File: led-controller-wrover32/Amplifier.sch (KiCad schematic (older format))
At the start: 5 parts, among them J11 Conn_01x02, U5 MAX98357A

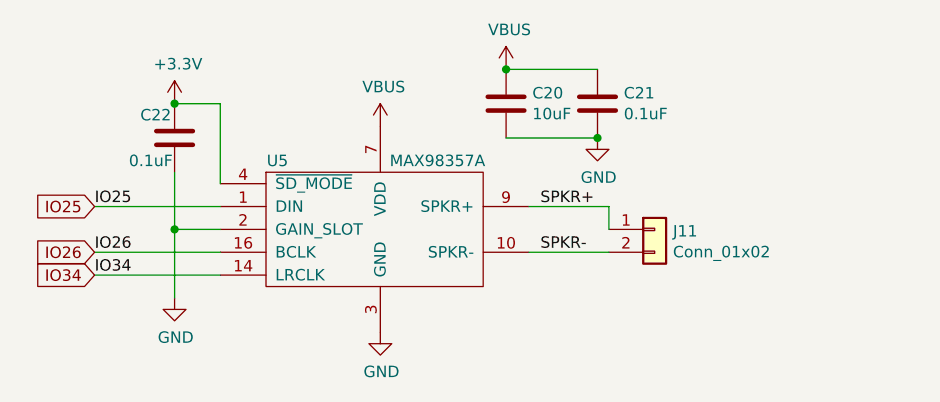
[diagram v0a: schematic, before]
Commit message: Fixed microphone, fan PWM and speaker
The ground was not hooked up to the microphone due to an issue with the
footprint.

The PWM pin was also used by the microphone.  Moved PWM pin to IO 5 which is
also shared with 5V output.

The speaker LR clock was using IO34 which is input only.  Moved to IO33 which
is also shared with a 5V output.

Updated revision to 3.0.1.
Fixed page settings, updated dates and revisions.

Signed-off-by: Aaron Williams <aaron.w2@gmail.com>
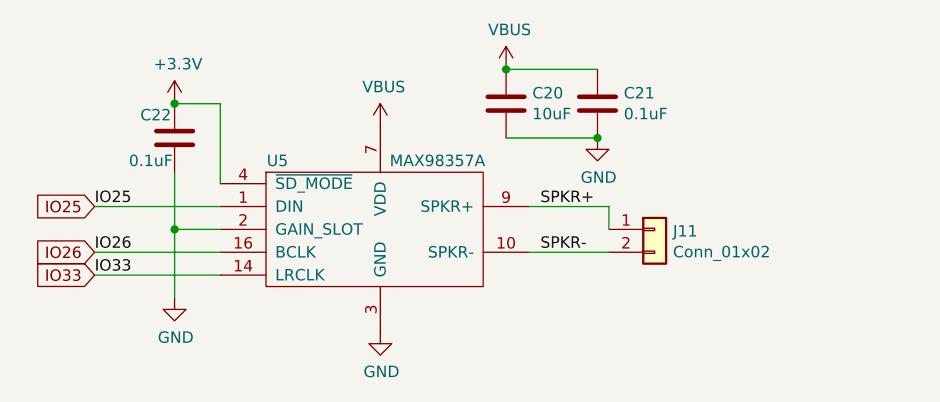
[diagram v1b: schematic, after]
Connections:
- net IO34 renamed IO33
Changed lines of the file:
@@
 	3200 3400 2650 3400
 Text Label 2650 3400 0    50   ~ 0
-IO34
+IO33
 Text GLabel 2650 3100 0    50   Input ~ 0
 IO25
@@
 IO26
 Text GLabel 2650 3400 0    50   Input ~ 0
-IO34
+IO33
 $Comp
 L Device:C C22

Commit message: Minor changes.
Signed-off-by: Aaron Williams <aaron.w2@gmail.com>
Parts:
- C20: MFR (none) -> Samsung; MPN (none) -> CL21B106KOQNNNE; SPN (none) -> 1276-2872-1-ND; SPR (none) -> Digikey; SPURL (none) -> -
- C21, C22: MFR (none) -> AVX; MPN (none) -> 06035C104K4Z4A; SPN (none) -> 478-10679-1-ND; SPR (none) -> Digikey; SPURL (none) -> -
- J11: value Conn_01x02 -> BM02B-SRSS-TB(LF)(SN)
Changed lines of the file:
@@
 U 1 1 5DB543D3
 P 3900 3200
-F 0 "U5" H 3450 3500 50  0000 C CNN
-F 1 "MAX98357A" H 4150 3500 50  0000 C CNN
-F 2 "Aaron:VQFN-16-1EP_3x3mm_P0.5mm_EP1.68x1.68mm" H 3900 3200 50  0001 C CNN
-F 3 "https://datasheets.maximintegrated.com/en/ds/MAX98357A-MAX98357B.pdf" H 3900 3200 50  0001 C CNN
-F 4 "Maxim Integrated" H 3900 3200 50  0001 C CNN "MFR"
-F 5 "MAX98357AETE+T" H 3900 3200 50  0001 C CNN "MPN"
-F 6 "Digikey" H 3900 3200 50  0001 C CNN "SPR"
-F 7 "MAX98357AETE+TCT-ND" H 3900 3200 50  0001 C CNN "SPN"
-F 8 "https://www.digikey.com/products/en/integrated-circuits-ics/linear-amplifiers-audio/742?k=MAX98357A&k=&pkeyword=MAX98357A&sv=0&pv7=2&pv1291=108687&pv16=108891&sf=0&FV=-8%7C742&quantity=&ColumnSort=0&page=1&pageSize=500" H 3900 3200 50  0001 C CNN "SPURL"
+F 0 "U5" H 3450 3500 50 0000 C CNN
+F 1 "MAX98357A" H 4150 3500 50 0000 C CNN
+F 2 "Aaron:VQFN-16-1EP_3x3mm_P0.5mm_EP1.68x1.68mm" H 3900 3200 50 0001 C CNN
+F 3 "https://datasheets.maximintegrated.com/en/ds/MAX98357A-MAX98357B.pdf" H 3900 3200 50 0001 C CNN
+F 4 "Maxim Integrated" H 3900 3200 50 0001 C CNN "MFR"
+F 5 "MAX98357AETE+T" H 3900 3200 50 0001 C CNN "MPN"
+F 6 "Digikey" H 3900 3200 50 0001 C CNN "SPR"
+F 7 "MAX98357AETE+TCT-ND" H 3900 3200 50 0001 C CNN "SPN"
+F 8 "https://www.digikey.com/products/en/integrated-circuits-ics/linear-amplifiers-audio/742?k=MAX98357A&k=&pkeyword=MAX98357A&sv=0&pv7=2&pv1291=108687&pv16=108891&sf=0&FV=-8%7C742&quantity=&ColumnSort=0&page=1&pageSize=500" H 3900 3200 50 0001 C CNN "SPURL"
 	1    3900 3200
 	1    0    0    -1
@@
 U 1 1 5DB55B9D
 P 4450 2650
-F 0 "C20" H 4565 2696 50  0000 L CNN
-F 1 "10uF" H 4565 2605 50  0000 L CNN
-F 2 "Capacitor_SMD:C_0805_2012Metric" H 4488 2500 50  0001 C CNN
-F 3 "~" H 4450 2650 50  0001 C CNN
+F 0 "C20" H 4565 2696 50 0000 L CNN
+F 1 "10uF" H 4565 2605 50 0000 L CNN
+F 2 "Capacitor_SMD:C_0805_2012Metric" H 4488 2500 50 0001 C CNN
+F 3 "http://www.samsungsem.com/kr/support/product-search/mlcc/CL21B106KOQNNNE.jsp" H 4450 2650 50 0001 C CNN
+F 4 "Samsung" H 0 0 50 0001 C CNN "MFR"
+F 5 "CL21B106KOQNNNE" H 0 0 50 0001 C CNN "MPN"
+F 6 "Digikey" H 0 0 50 0001 C CNN "SPR"
+F 7 "1276-2872-1-ND" H 0 0 50 0001 C CNN "SPN"
+F 8 "-" H 0 0 50 0001 C CNN "SPURL"
 	1    4450 2650
 	1    0    0    -1
@@
 U 1 1 5DB56E4D
 P 4850 2650
-F 0 "C21" H 4965 2696 50  0000 L CNN
-F 1 "0.1uF" H 4965 2605 50  0000 L CNN
-F 2 "Capacitor_SMD:C_0603_1608Metric" H 4888 2500 50  0001 C CNN
-F 3 "~" H 4850 2650 50  0001 C CNN
+F 0 "C21" H 4965 2696 50 0000 L CNN
+F 1 "0.1uF" H 4965 2605 50 0000 L CNN
+F 2 "Capacitor_SMD:C_0603_1608Metric" H 4888 2500 50 0001 C CNN
+F 3 "http://datasheets.avx.com/FlexitermMLCC.pdf" H 4850 2650 50 0001 C CNN
+F 4 "AVX" H 0 0 50 0001 C CNN "MFR"
+F 5 "06035C104K4Z4A" H 0 0 50 0001 C CNN "MPN"
+F 6 "Digikey" H 0 0 50 0001 C CNN "SPR"
+F 7 "478-10679-1-ND" H 0 0 50 0001 C CNN "SPN"
+F 8 "-" H 0 0 50 0001 C CNN "SPURL"
 	1    4850 2650
 	1    0    0    -1
@@
 U 1 1 5DB5770E
 P 3900 3650
-F 0 "#PWR0116" H 3900 3400 50  0001 C CNN
-F 1 "GND" H 3905 3477 50  0000 C CNN
-F 2 "" H 3900 3650 50  0001 C CNN
-F 3 "" H 3900 3650 50  0001 C CNN
+F 0 "#PWR0116" H 3900 3400 50 0001 C CNN
+F 1 "GND" H 3905 3477 50 0000 C CNN
+F 2 "" H 3900 3650 50 0001 C CNN
+F 3 "" H 3900 3650 50 0001 C CNN
 	1    3900 3650
 	1    0    0    -1
@@
 U 1 1 5DB58235
 P 3000 3500
-F 0 "#PWR0117" H 3000 3250 50  0001 C CNN
-F 1 "GND" H 3005 3327 50  0000 C CNN
-F 2 "" H 3000 3500 50  0001 C CNN
-F 3 "" H 3000 3500 50  0001 C CNN
+F 0 "#PWR0117" H 3000 3250 50 0001 C CNN
+F 1 "GND" H 3005 3327 50 0000 C CNN
+F 2 "" H 3000 3500 50 0001 C CNN
+F 3 "" H 3000 3500 50 0001 C CNN
 	1    3000 3500
 	1    0    0    -1
 $EndComp
-Wire Wire Line
-	3200 3200 3000 3200
-Wire Wire Line
-	3000 3200 3000 3500
 $Comp
 L power:+3.3V #PWR0118
 U 1 1 5DB59262
 P 3000 2650
-F 0 "#PWR0118" H 3000 2500 50  0001 C CNN
-F 1 "+3.3V" H 3015 2823 50  0000 C CNN
-F 2 "" H 3000 2650 50  0001 C CNN
-F 3 "" H 3000 2650 50  0001 C CNN
+F 0 "#PWR0118" H 3000 2500 50 0001 C CNN
+F 1 "+3.3V" H 3015 2823 50 0000 C CNN
+F 2 "" H 3000 2650 50 0001 C CNN
+F 3 "" H 3000 2650 50 0001 C CNN
 	1    3000 2650
 	1    0    0    -1
 $EndComp
-Wire Wire Line
-	4450 2500 4850 2500
 $Comp
 L power:GND #PWR0119
 U 1 1 5DB5D003
 P 4850 2800
-F 0 "#PWR0119" H 4850 2550 50  0001 C CNN
-F 1 "GND" H 4855 2627 50  0000 C CNN
-F 2 "" H 4850 2800 50  0001 C CNN
-F 3 "" H 4850 2800 50  0001 C CNN
+F 0 "#PWR0119" H 4850 2550 50 0001 C CNN
+F 1 "GND" H 4855 2627 50 0000 C CNN
+F 2 "" H 4850 2800 50 0001 C CNN
+F 3 "" H 4850 2800 50 0001 C CNN
 	1    4850 2800
 	1    0    0    -1
 $EndComp
-Wire Wire Line
-	4850 2800 4450 2800
-Connection ~ 4850 2800
 $Comp
 L power:VBUS #PWR0120
 U 1 1 5DB5DCA0
 P 4450 2500
-F 0 "#PWR0120" H 4450 2350 50  0001 C CNN
-F 1 "VBUS" H 4465 2673 50  0000 C CNN
-F 2 "" H 4450 2500 50  0001 C CNN
-F 3 "" H 4450 2500 50  0001 C CNN
+F 0 "#PWR0120" H 4450 2350 50 0001 C CNN
+F 1 "VBUS" H 4465 2673 50 0000 C CNN
+F 2 "" H 4450 2500 50 0001 C CNN
+F 3 "" H 4450 2500 50 0001 C CNN
 	1    4450 2500
 	1    0    0    -1
 $EndComp
-Connection ~ 4450 2500
 $Comp
 L power:VBUS #PWR0121
 U 1 1 5DB5E7EE
 P 3900 2750
-F 0 "#PWR0121" H 3900 2600 50  0001 C CNN
-F 1 "VBUS" H 3915 2923 50  0000 C CNN
-F 2 "" H 3900 2750 50  0001 C CNN
-F 3 "" H 3900 2750 50  0001 C CNN
+F 0 "#PWR0121" H 3900 2600 50 0001 C CNN
+F 1 "VBUS" H 3915 2923 50 0000 C CNN
+F 2 "" H 3900 2750 50 0001 C CNN
+F 3 "" H 3900 2750 50 0001 C CNN
 	1    3900 2750
 	1    0    0    -1
@@
 U 1 1 5DBCE011
 P 5100 3200
-F 0 "J11" H 5180 3192 50  0000 L CNN
-F 1 "Conn_01x02" H 5180 3101 50  0000 L CNN
-F 2 "Aaron:JST_SH_BM02B-SRSS-TB_1x02-1MP_P1.00mm_Vertical" H 5100 3200 50  0001 C CNN
-F 3 "https://media.digikey.com/pdf/Data%20Sheets/JST%20PDFs/SR%20Connector.pdf" H 5100 3200 50  0001 C CNN
-F 4 "JST Sales America Inc." H 5100 3200 50  0001 C CNN "MFR"
-F 5 "BM02B-SRSS-TB(LF)(SN)" H 5100 3200 50  0001 C CNN "MPN"
-F 6 "Digikey" H 5100 3200 50  0001 C CNN "SPR"
-F 7 "455-1788-1-ND" H 5100 3200 50  0001 C CNN "SPN"
-F 8 "https://www.digikey.com/product-detail/en/jst-sales-america-inc/BM02B-SRSS-TB-LF-SN/455-1788-1-ND/926859" H 5100 3200 50  0001 C CNN "SPURL"
+F 0 "J11" H 5180 3192 50 0000 L CNN
+F 1 "BM02B-SRSS-TB(LF)(SN)" H 5180 3101 50 0000 L CNN
+F 2 "Aaron:JST_SH_BM02B-SRSS-TB_1x02-1MP_P1.00mm_Vertical" H 5100 3200 50 0001 C CNN
+F 3 "https://media.digikey.com/pdf/Data%20Sheets/JST%20PDFs/SR%20Connector.pdf" H 5100 3200 50 0001 C CNN
+F 4 "JST Sales America Inc." H 5100 3200 50 0001 C CNN "MFR"
+F 5 "BM02B-SRSS-TB(LF)(SN)" H 5100 3200 50 0001 C CNN "MPN"
+F 6 "Digikey" H 5100 3200 50 0001 C CNN "SPR"
+F 7 "455-1788-1-ND" H 5100 3200 50 0001 C CNN "SPN"
+F 8 "https://www.digikey.com/product-detail/en/jst-sales-america-inc/BM02B-SRSS-TB-LF-SN/455-1788-1-ND/926859" H 5100 3200 50 0001 C CNN "SPURL"
 	1    5100 3200
 	1    0    0    -1
 $EndComp
-Wire Wire Line
-	3200 3100 2650 3100
+$Comp
+L Device:C C22
+U 1 1 5E040A75
+P 3000 2800
+F 0 "C22" H 2850 2900 50 0000 L CNN
+F 1 "0.1uF" H 2800 2700 50 0000 L CNN
+F 2 "Capacitor_SMD:C_0603_1608Metric" H 3038 2650 50 0001 C CNN
+F 3 "http://datasheets.avx.com/FlexitermMLCC.pdf" H 3000 2800 50 0001 C CNN
+F 4 "AVX" H 0 0 50 0001 C CNN "MFR"
+F 5 "06035C104K4Z4A" H 0 0 50 0001 C CNN "MPN"
+F 6 "Digikey" H 0 0 50 0001 C CNN "SPR"
+F 7 "478-10679-1-ND" H 0 0 50 0001 C CNN "SPN"
+F 8 "-" H 0 0 50 0001 C CNN "SPURL"
+	1    3000 2800
+	1    0    0    -1
+$EndComp
 Text Label 2650 3100 0    50   ~ 0
 IO25
-Wire Wire Line
-	3200 3300 2650 3300
 Text Label 2650 3300 0    50   ~ 0
 IO26
-Wire Wire Line
-	3200 3400 2650 3400
 Text Label 2650 3400 0    50   ~ 0
 IO33
@@
 Text GLabel 2650 3400 0    50   Input ~ 0
 IO33
-$Comp
-L Device:C C22
-U 1 1 5E040A75
-P 3000 2800
-F 0 "C22" H 2850 2900 50  0000 L CNN
-F 1 "0.1uF" H 2800 2700 50  0000 L CNN
-F 2 "Capacitor_SMD:C_0603_1608Metric" H 3038 2650 50  0001 C CNN
-F 3 "~" H 3000 2800 50  0001 C CNN
-	1    3000 2800
-	1    0    0    -1
-$EndComp
+Text Label 4600 3100 0    50   ~ 0
+SPKR+
+Text Label 4600 3300 0    50   ~ 0
+SPKR-
+Wire Wire Line
+	3200 3200 3000 3200
+Wire Wire Line
+	3000 3200 3000 3500
+Wire Wire Line
+	4450 2500 4850 2500
+Wire Wire Line
+	4850 2800 4450 2800
+Wire Wire Line
+	3200 3100 2650 3100
+Wire Wire Line
+	3200 3300 2650 3300
+Wire Wire Line
+	3200 3400 2650 3400
 Wire Wire Line
 	3000 2650 3200 2650
 Wire Wire Line
 	3200 2650 3200 3000
-Connection ~ 3000 2650
 Wire Wire Line
 	3000 3200 3000 2950
-Connection ~ 3000 3200
-Text Label 4600 3100 0    50   ~ 0
-SPKR+
-Text Label 4600 3300 0    50   ~ 0
-SPKR-
 Wire Wire Line
 	4900 3100 4900 3200
@@
 Wire Wire Line
 	4550 3300 4900 3300
+Connection ~ 4850 2800
+Connection ~ 4450 2500
+Connection ~ 3000 2650
+Connection ~ 3000 3200
 $EndSCHEMATC
